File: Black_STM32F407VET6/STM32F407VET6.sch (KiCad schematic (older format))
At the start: 89 parts, among them J1 T0, J10 - HotBed +, J11 Heater0, J12 X-, J13 Y-, J14 Z-, J15 Z+, J16 USB_B, J17 LeftSpi, J18 EXTRAPINS, J19 12Vinput, J2 T1, J20 5VOut, J23 EXP2, J24 LCD2004, J25 Bottom, J26 Right, J28 LIGHTS, J29 Z, J3 TB, J30 Z, J38 X, J39 Y, J4 TC, J41 E0, J43 Heater1, J44 COM, J47 I2C, J48 SPI, J49 SPI, J5 + VIN -, J50 SDIO, J51 Servo, J52 Servo, J53 PowerSelect, J54 Power, J55 PD11, J56 Power, J6 Fan3, J7 Fan2, J8 Fan1, J9 Fan0, Q12 IRLR8726PBF, Q13 IRLR8726PBF, Q14 IRLR8726PBF, Q4 IRLML0030TRPBF, Q6 IRLML0030TRPBF, Q7 IRLML0030TRPBF, Q8 IRLML0030TRPBF, SW1 Boot0, U1 LeftAnalog, U2 Left5V, U3 BuckConvertor, U4 LM2901, U5 AT24CS01-SSHM, U6 LM2901

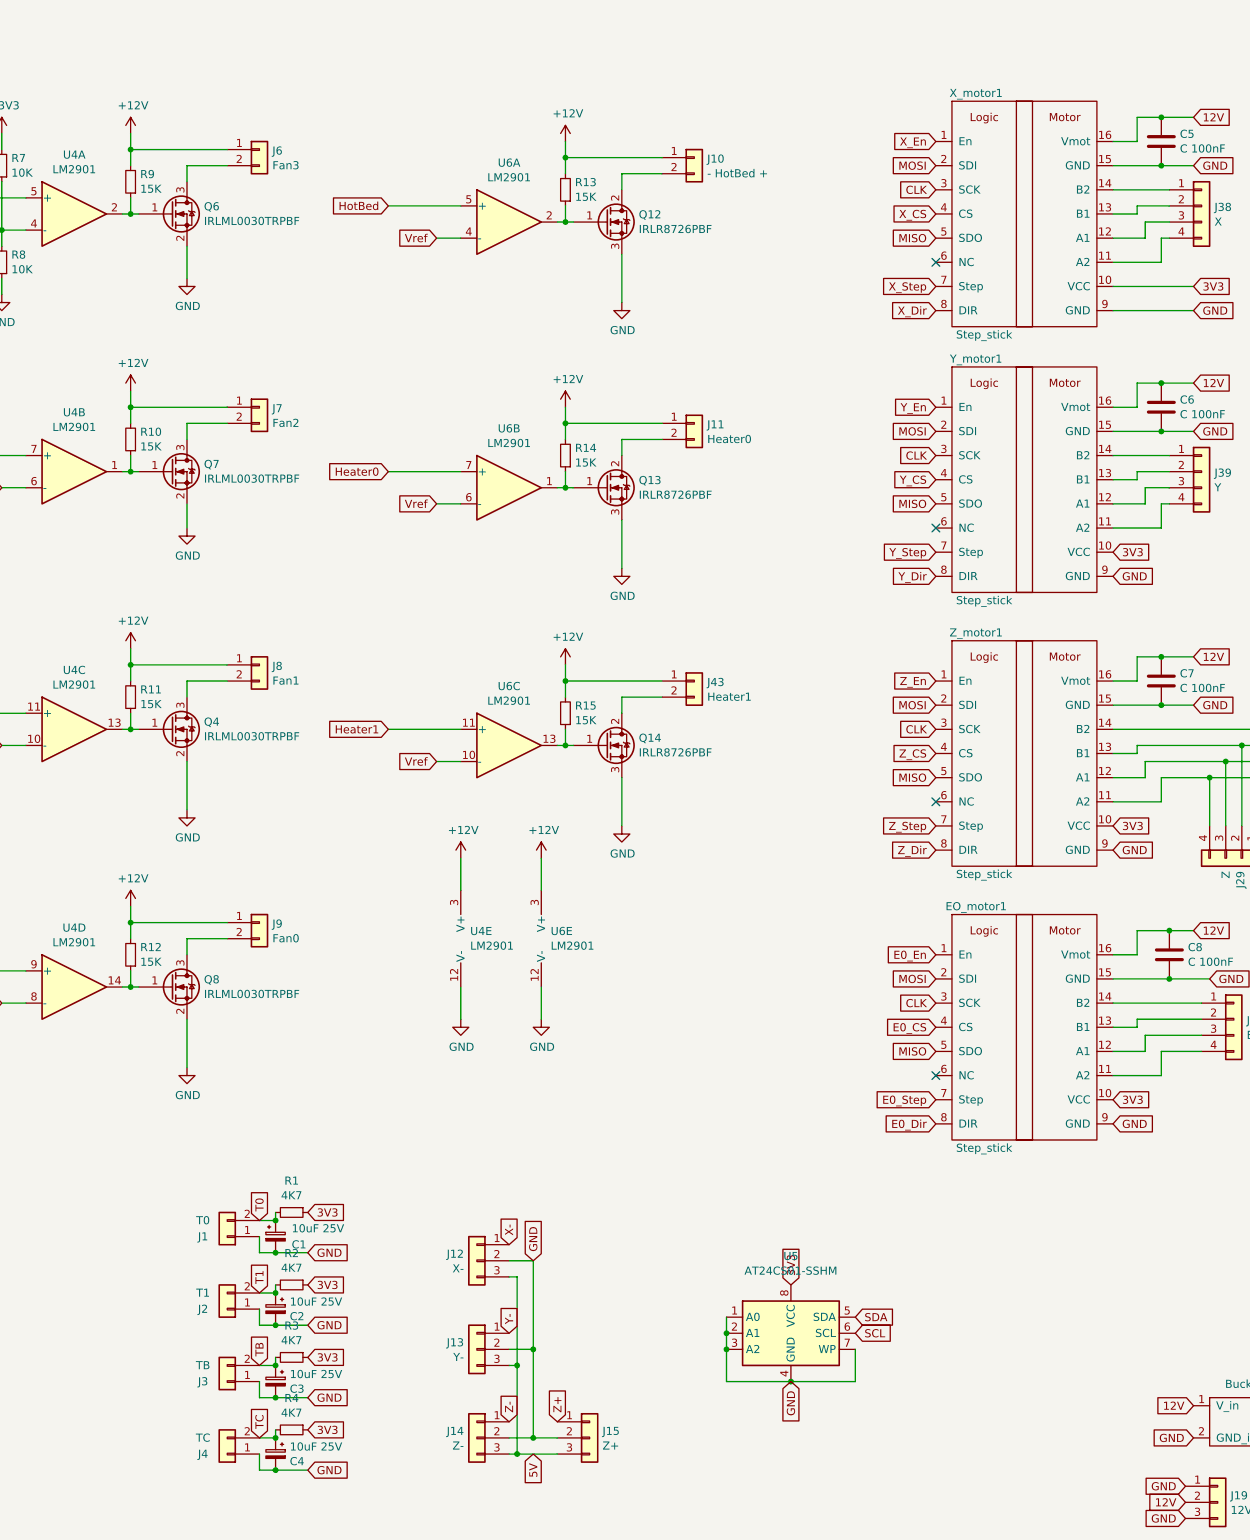
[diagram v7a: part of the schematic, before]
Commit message: //Forgot to save Fan separated power rail to allow different voltage Moved border to fabrication layer to prepare for milling
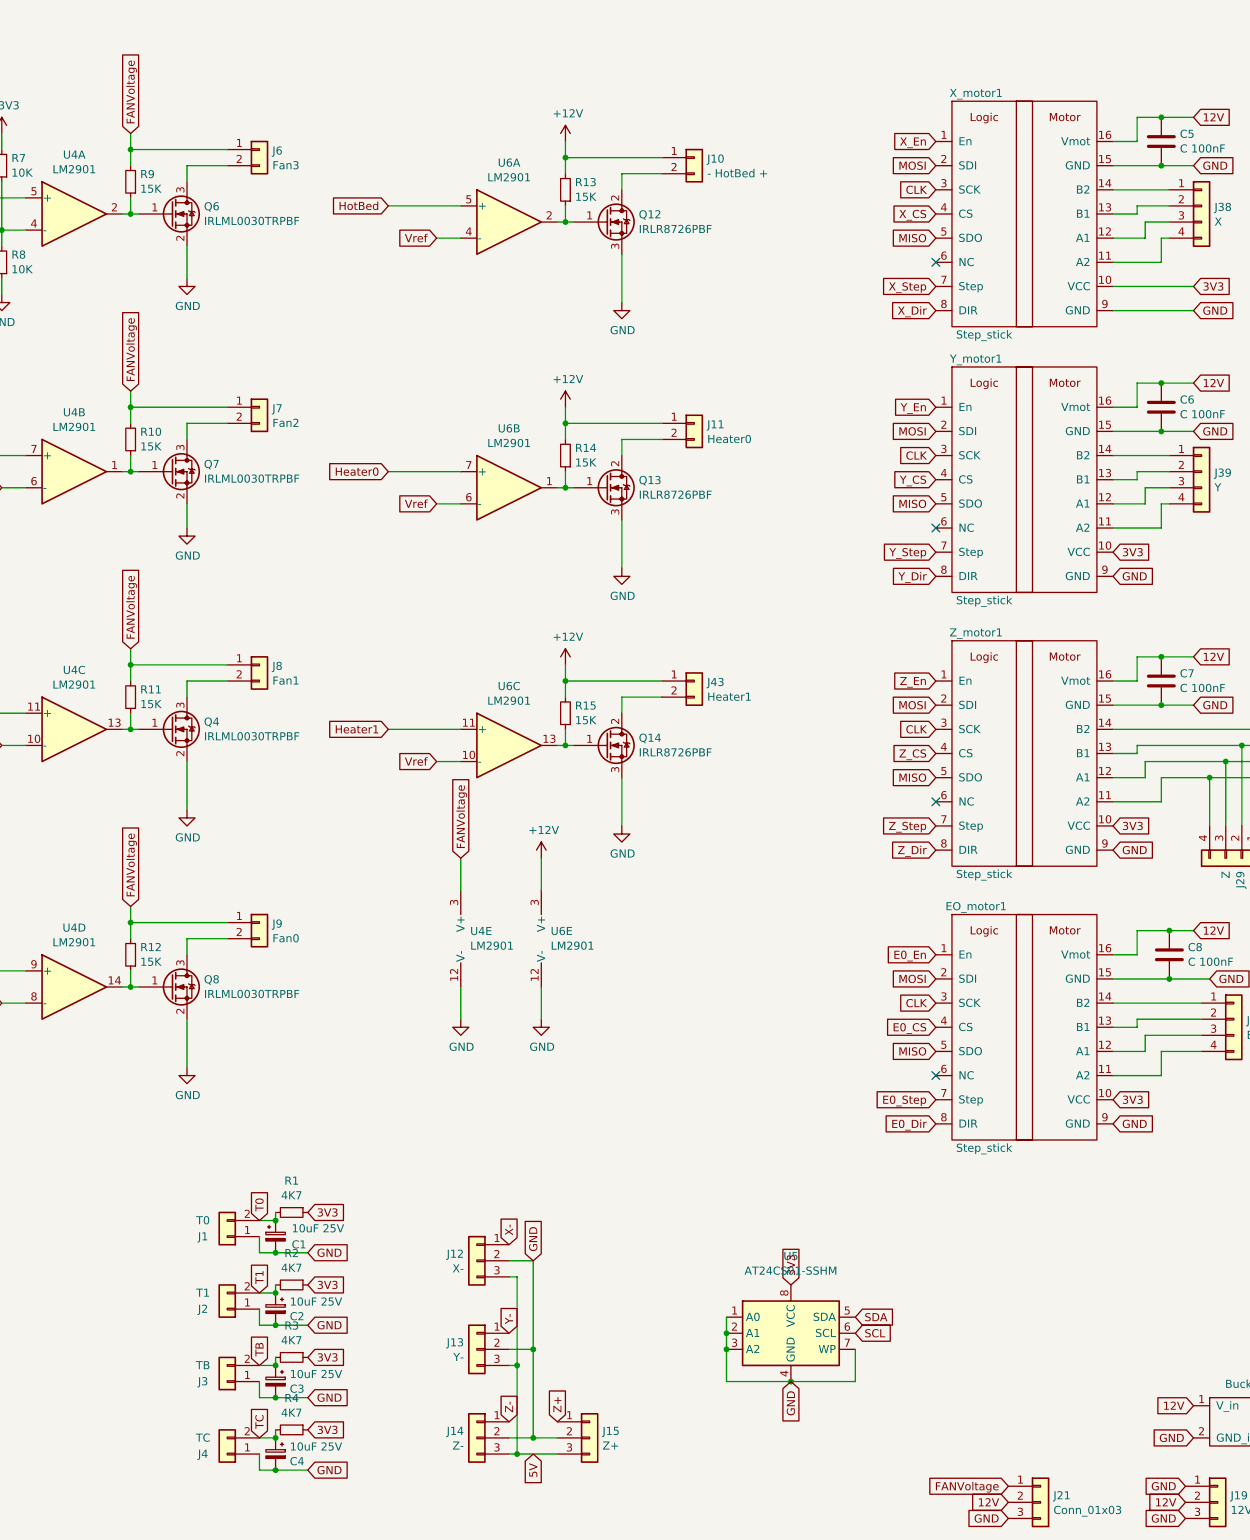
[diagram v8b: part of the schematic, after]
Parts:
- added J21: Conn_01x03, Connector_PinHeader_2.54mm:PinHeader_1x03_P2.54mm_Vertical, symbol Connector_Generic:Conn_01x03
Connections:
- net +12V: now also J21.2 (Pin_2); no longer J6.1 (Pin_1), J7.1 (Pin_1), J8.1 (Pin_1), J9.1 (Pin_1), R10.2, R11.2, R12.2, R9.2, U4.3 (V+)
- net GND: now also J21.3 (Pin_3)
- new net FANVoltage: J21.1 (Pin_1), J6.1 (Pin_1), J7.1 (Pin_1), J8.1 (Pin_1), J9.1 (Pin_1), R10.2, R11.2, R12.2, R9.2, U4.3 (V+)
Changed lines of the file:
@@
 Wire Wire Line
 	1900 1350 1900 1250
-$Comp
-L power:+12V #PWR0112
-U 1 1 5D342768
-P 1900 1250
-F 0 "#PWR0112" H 1915 1515 50  0001 C CNN
-F 1 "+12V" H 1915 1423 50  0000 C CNN
-F 2 "" H 1900 1250 50  0001 C CNN
-F 3 "" H 1900 1250 50  0001 C CNN
-	1    1900 1250
-	1    0    0    -1
-$EndComp
 Wire Wire Line
 	800  3250 1250 3250
@@
 Wire Wire Line
 	1900 2950 1900 2850
-$Comp
-L power:+12V #PWR03
-U 1 1 5D55B2AC
-P 1900 2850
-F 0 "#PWR03" H 1915 3115 50  0001 C CNN
-F 1 "+12V" H 1915 3023 50  0000 C CNN
-F 2 "" H 1900 2850 50  0001 C CNN
-F 3 "" H 1900 2850 50  0001 C CNN
-	1    1900 2850
-	1    0    0    -1
-$EndComp
 Text GLabel 950  1850 0    50   Input ~ 0
 Vref
@@
 Wire Wire Line
 	1900 4550 1900 4450
-$Comp
-L power:+12V #PWR04
-U 1 1 5D5C4003
-P 1900 4450
-F 0 "#PWR04" H 1915 4715 50  0001 C CNN
-F 1 "+12V" H 1915 4623 50  0000 C CNN
-F 2 "" H 1900 4450 50  0001 C CNN
-F 3 "" H 1900 4450 50  0001 C CNN
-	1    1900 4450
-	1    0    0    -1
-$EndComp
 Text GLabel 1100 5050 0    50   Input ~ 0
 Vref
@@
 Wire Wire Line
 	1900 6150 1900 6050
-$Comp
-L power:+12V #PWR05
-U 1 1 5D613EBE
-P 1900 6050
-F 0 "#PWR05" H 1915 6315 50  0001 C CNN
-F 1 "+12V" H 1915 6223 50  0000 C CNN
-F 2 "" H 1900 6050 50  0001 C CNN
-F 3 "" H 1900 6050 50  0001 C CNN
-	1    1900 6050
-	1    0    0    -1
-$EndComp
 Text GLabel 1100 6650 0    50   Input ~ 0
 Vref
@@
 $EndComp
 $Comp
-L power:+12V #PWR08
-U 1 1 5D640870
-P 3950 5750
-F 0 "#PWR08" H 3965 6015 50  0001 C CNN
-F 1 "+12V" H 3965 5923 50  0000 C CNN
-F 2 "" H 3950 5750 50  0001 C CNN
-F 3 "" H 3950 5750 50  0001 C CNN
-	1    3950 5750
-	1    0    0    -1
-$EndComp
-$Comp
 L power:GND #PWR09
 U 1 1 5D640E8A
@@
 	1    0    0    -1
 $EndComp
+$Comp
+L Connector_Generic:Conn_01x03 J21
+U 1 1 5D5586B8
+P 7550 9750
+F 0 "J21" H 7630 9792 50  0000 L CNN
+F 1 "Conn_01x03" H 7630 9701 50  0000 L CNN
+F 2 "Connector_PinHeader_2.54mm:PinHeader_1x03_P2.54mm_Vertical" H 7550 9750 50  0001 C CNN
+F 3 "~" H 7550 9750 50  0001 C CNN
+	1    7550 9750
+	1    0    0    -1
+$EndComp
+Text GLabel 7350 9750 0    50   Input ~ 0
+12V
+Text GLabel 7350 9850 0    50   Input ~ 0
+GND
+Text GLabel 7350 9650 0    50   Input ~ 0
+FANVoltage
+Text GLabel 1900 4450 1    50   Input ~ 0
+FANVoltage
+Text GLabel 1900 6050 1    50   Input ~ 0
+FANVoltage
+Text GLabel 1900 2850 1    50   Input ~ 0
+FANVoltage
+Text GLabel 1900 1250 1    50   Input ~ 0
+FANVoltage
+Text GLabel 3950 5750 1    50   Input ~ 0
+FANVoltage
 $EndSCHEMATC
